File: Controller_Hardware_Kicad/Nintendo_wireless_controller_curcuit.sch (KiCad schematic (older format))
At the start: 23 parts, among them IC1 ATTINY2313-S, J1 BATT, J2 NRF_conn, U1 MAX1811, U2 LP5951MF-3.3, X1 USB-MB-S, X2 8MHz, sw1 CONN_2

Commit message: configured max1811 pin connections again.. and again
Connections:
- net +5V: now also U1.1 (SELV)
- net GND: no longer U1.1 (SELV)
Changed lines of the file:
@@
-EESchema Schematic File Version 2  date 19-06-2012 16:43:49
+EESchema Schematic File Version 2  date 19-06-2012 16:48:53
 LIBS:power
 LIBS:device
@@
 Comment4 ""
 $EndDescr
-Wire Wire Line
-	2550 7100 2550 6700
-Wire Wire Line
-	4450 7200 4800 7200
-Wire Wire Line
-	4800 7200 4800 7150
-Wire Wire Line
-	4800 6750 4800 6700
-Wire Wire Line
-	4800 6700 3900 6700
+$Comp
+L +5V #PWR01
+U 1 1 4FE08C10
+P 2550 6650
+F 0 "#PWR01" H 2550 6740 20  0001 C CNN
+F 1 "+5V" H 2550 6740 30  0000 C CNN
+	1    2550 6650
+	1    0    0    -1
+$EndComp
+Wire Wire Line
+	2550 6700 2550 6650
+Wire Wire Line
+	2550 7100 2550 6800
+Connection ~ 4450 7200
+Wire Wire Line
+	4450 7150 4450 7300
+Wire Wire Line
+	5150 4150 5150 4200
+Wire Wire Line
+	5150 4200 5200 4200
+Connection ~ 2600 3000
+Wire Wire Line
+	2800 3000 2350 3000
+Wire Wire Line
+	2800 3000 2800 3150
+Wire Wire Line
+	3300 850  3300 700
+Wire Wire Line
+	8300 2300 8300 2450
+Wire Wire Line
+	6750 2700 6750 2450
+Wire Wire Line
+	4450 3500 4450 3600
+Connection ~ 2600 3550
+Wire Wire Line
+	2800 3550 2350 3550
+Wire Wire Line
+	5150 4500 5150 4400
+Wire Wire Line
+	5150 4400 5200 4400
+Wire Wire Line
+	7150 6400 7550 6400
+Wire Wire Line
+	1500 5700 1500 5350
+Wire Wire Line
+	1500 5350 1300 5350
+Wire Wire Line
+	8300 2450 8050 2450
+Connection ~ 9750 5750
+Wire Wire Line
+	10150 5850 10150 5750
+Wire Wire Line
+	10150 5750 9750 5750
+Connection ~ 7950 6000
+Wire Wire Line
+	8100 6100 7950 6100
+Wire Wire Line
+	7550 5600 7550 5400
+Wire Wire Line
+	8900 6600 8900 6850
+Connection ~ 2150 5350
+Wire Wire Line
+	2150 5350 2700 5350
+Wire Wire Line
+	2150 6500 2700 6500
+Wire Wire Line
+	2150 6350 2150 6500
+Wire Wire Line
+	2150 5300 2150 5400
+Wire Wire Line
+	4450 6600 4450 6750
+Wire Wire Line
+	3900 7000 4000 7000
+Connection ~ 4000 7000
+Wire Wire Line
+	4000 7000 4000 7100
+Connection ~ 2550 6800
+Wire Wire Line
+	2550 6800 2700 6800
+Connection ~ 5700 7000
+Wire Wire Line
+	5700 7150 5700 6900
+Wire Wire Line
+	5350 7000 5700 7000
+Wire Wire Line
+	5700 6500 5700 6700
+Wire Wire Line
+	5700 6700 5800 6700
+Wire Wire Line
+	1750 5300 1750 5450
+Wire Wire Line
+	1750 5450 1300 5450
+Connection ~ 2400 1750
+Wire Wire Line
+	2300 1750 3200 1750
+Wire Wire Line
+	3200 1750 3200 2000
+Wire Wire Line
+	3200 2000 3300 2000
+Wire Wire Line
+	2400 1850 2400 1750
+Wire Wire Line
+	1900 2550 1750 2550
+Wire Wire Line
+	1750 1750 1900 1750
+Connection ~ 1750 2550
+Wire Wire Line
+	2400 2450 2400 2550
+Wire Wire Line
+	3300 2200 3200 2200
+Wire Wire Line
+	3200 2550 3200 2200
+Wire Wire Line
+	2300 2550 3200 2550
+Connection ~ 2400 2550
+Wire Wire Line
+	3300 1350 3300 1700
+Wire Wire Line
+	5700 6900 5800 6900
+Wire Wire Line
+	5350 6600 5700 6600
+Connection ~ 5700 6600
+Wire Wire Line
+	2700 6700 2550 6700
+Wire Wire Line
+	2550 7000 2700 7000
+Connection ~ 2550 7000
+Wire Wire Line
+	3900 6400 4000 6400
+Wire Wire Line
+	4000 6400 4000 6350
+Connection ~ 4450 6700
+Wire Wire Line
+	2150 5900 2150 5950
+Wire Wire Line
+	2700 5350 2700 6400
+Wire Wire Line
+	2050 6450 2150 6450
+Connection ~ 2150 6450
+Wire Wire Line
+	9750 6000 9700 6000
+Wire Wire Line
+	9750 5550 9750 6000
+Wire Wire Line
+	10150 6250 10150 6500
+Wire Wire Line
+	7550 6400 7550 6550
+Wire Wire Line
+	7550 6000 7550 5800
+Wire Wire Line
+	6750 2450 7250 2450
+Wire Wire Line
+	7950 6100 7950 6000
+Wire Wire Line
+	8100 6000 7150 6000
+Connection ~ 7550 6000
+Wire Wire Line
+	2600 3650 2600 3550
+Wire Wire Line
+	1750 2700 1750 1750
+Wire Wire Line
+	5600 5200 5650 5200
+Wire Wire Line
+	5650 5200 5650 5300
+Wire Wire Line
+	5600 5000 5650 5000
+Wire Wire Line
+	5650 5000 5650 4950
+Wire Wire Line
+	4450 1400 4450 1250
+Wire Wire Line
+	2350 3000 2350 3150
 Wire Wire Line
 	2600 3000 2600 2950
 Wire Wire Line
-	2350 3150 2350 3000
-Wire Wire Line
-	4450 1400 4450 1250
-Wire Wire Line
-	5650 4950 5650 5000
-Wire Wire Line
-	5650 5000 5600 5000
-Wire Wire Line
-	5650 5300 5650 5200
-Wire Wire Line
-	5650 5200 5600 5200
-Wire Wire Line
-	1750 2700 1750 1750
-Wire Wire Line
-	2600 3650 2600 3550
-Connection ~ 7550 6000
-Wire Wire Line
-	8100 6000 7150 6000
-Wire Wire Line
-	7950 6000 7950 6100
-Wire Wire Line
-	7250 2450 6750 2450
-Wire Wire Line
-	7550 6000 7550 5800
-Wire Wire Line
-	7550 6550 7550 6400
-Wire Wire Line
-	10150 6250 10150 6500
-Wire Wire Line
-	9750 5550 9750 6000
-Wire Wire Line
-	9750 6000 9700 6000
-Connection ~ 2150 6450
-Wire Wire Line
-	2050 6450 2150 6450
-Wire Wire Line
-	2700 6400 2700 5350
-Wire Wire Line
-	2150 5900 2150 5950
-Connection ~ 4450 6700
-Wire Wire Line
-	4000 6350 4000 6400
-Wire Wire Line
-	4000 6400 3900 6400
-Connection ~ 2550 7000
-Wire Wire Line
-	2550 7000 2700 7000
-Wire Wire Line
-	2550 6700 2700 6700
-Connection ~ 5700 6600
-Wire Wire Line
-	5350 6600 5700 6600
-Wire Wire Line
-	5800 6900 5700 6900
-Wire Wire Line
-	3300 1350 3300 1700
-Connection ~ 2400 2550
-Wire Wire Line
-	2300 2550 3200 2550
-Wire Wire Line
-	3200 2550 3200 2200
-Wire Wire Line
-	3200 2200 3300 2200
-Wire Wire Line
-	2400 2450 2400 2550
-Connection ~ 1750 2550
-Wire Wire Line
-	1750 1750 1900 1750
-Wire Wire Line
-	1900 2550 1750 2550
-Wire Wire Line
-	2400 1850 2400 1750
-Wire Wire Line
-	3300 2000 3200 2000
-Wire Wire Line
-	3200 2000 3200 1750
-Wire Wire Line
-	3200 1750 2300 1750
-Connection ~ 2400 1750
-Wire Wire Line
-	1300 5450 1750 5450
-Wire Wire Line
-	1750 5450 1750 5300
-Wire Wire Line
-	5800 6700 5700 6700
-Wire Wire Line
-	5700 6700 5700 6500
-Wire Wire Line
-	5350 7000 5700 7000
-Wire Wire Line
-	5700 6900 5700 7150
-Connection ~ 5700 7000
-Wire Wire Line
-	2550 6800 2700 6800
-Connection ~ 2550 6800
-Wire Wire Line
-	4000 7100 4000 7000
-Connection ~ 4000 7000
-Wire Wire Line
-	4000 7000 3900 7000
-Wire Wire Line
-	4450 6600 4450 6750
-Wire Wire Line
-	2150 5300 2150 5400
-Wire Wire Line
-	2150 6350 2150 6500
-Wire Wire Line
-	2150 6500 2700 6500
-Wire Wire Line
-	2700 5350 2150 5350
-Connection ~ 2150 5350
-Wire Wire Line
-	8900 6600 8900 6850
-Wire Wire Line
-	7550 5600 7550 5400
-Wire Wire Line
-	7950 6100 8100 6100
-Connection ~ 7950 6000
-Wire Wire Line
-	9750 5750 10150 5750
-Wire Wire Line
-	10150 5750 10150 5850
-Connection ~ 9750 5750
-Wire Wire Line
-	8050 2450 8300 2450
-Wire Wire Line
-	1300 5350 1500 5350
-Wire Wire Line
-	1500 5350 1500 5700
-Wire Wire Line
-	7550 6400 7150 6400
-Wire Wire Line
-	5200 4400 5150 4400
-Wire Wire Line
-	5150 4400 5150 4500
-Wire Wire Line
-	2800 3550 2350 3550
-Connection ~ 2600 3550
-Wire Wire Line
-	4450 3500 4450 3600
-Wire Wire Line
-	6750 2450 6750 2700
-Wire Wire Line
-	8300 2450 8300 2300
-Wire Wire Line
-	3300 850  3300 700
-Wire Wire Line
-	2800 3150 2800 3000
-Wire Wire Line
-	2800 3000 2350 3000
-Connection ~ 2600 3000
-Wire Wire Line
-	5200 4200 5150 4200
-Wire Wire Line
-	5150 4200 5150 4150
-Wire Wire Line
-	4450 7150 4450 7300
-Connection ~ 4450 7200
+	3900 6700 4800 6700
+Wire Wire Line
+	4800 6700 4800 6750
+Wire Wire Line
+	4800 7150 4800 7200
+Wire Wire Line
+	4800 7200 4450 7200
 Text Notes 2850 6150 0    60   ~ 0
 100mA charge current = ca. 4hr charge time

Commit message: ahmmaghad! we forgot to connect the dataline to the controller
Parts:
- added P1: CONN_1, symbol CONN_1
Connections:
- net at IC1.6 ((CKOUT/XCK/INT0)PD2): now also P1.1

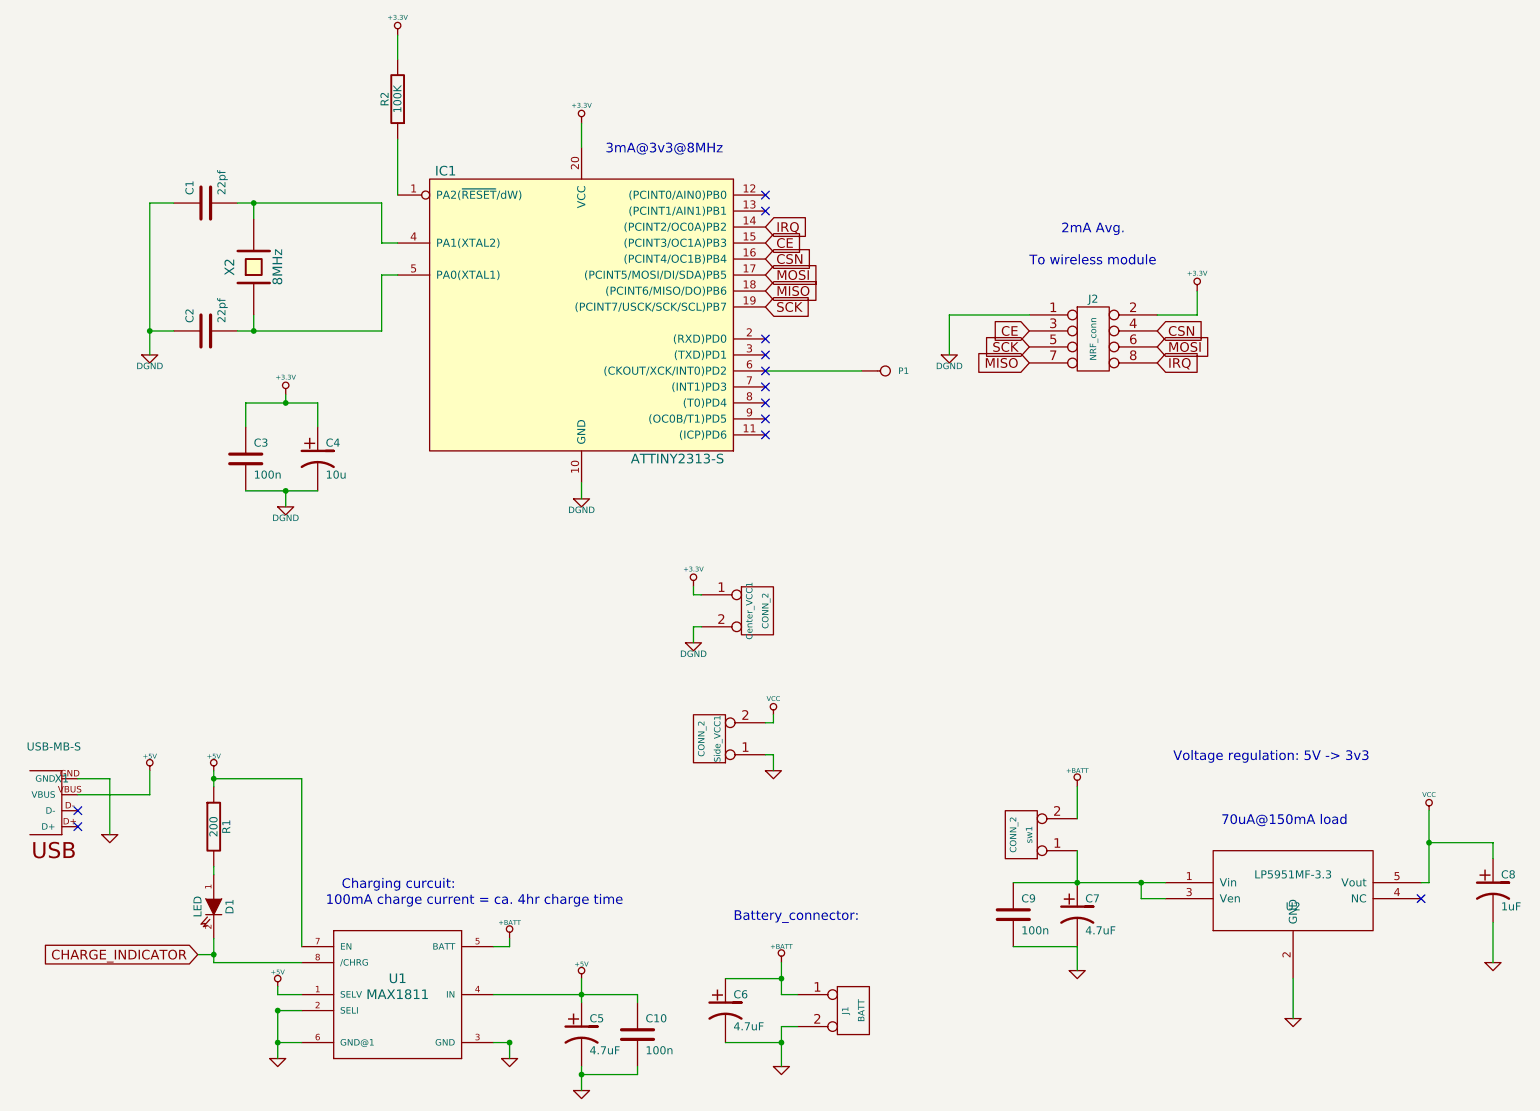
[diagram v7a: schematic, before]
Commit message: changed schematic to utilize attiny24 - still needs analog circuitry, netlisted and changed footprints, but didnt start layouting
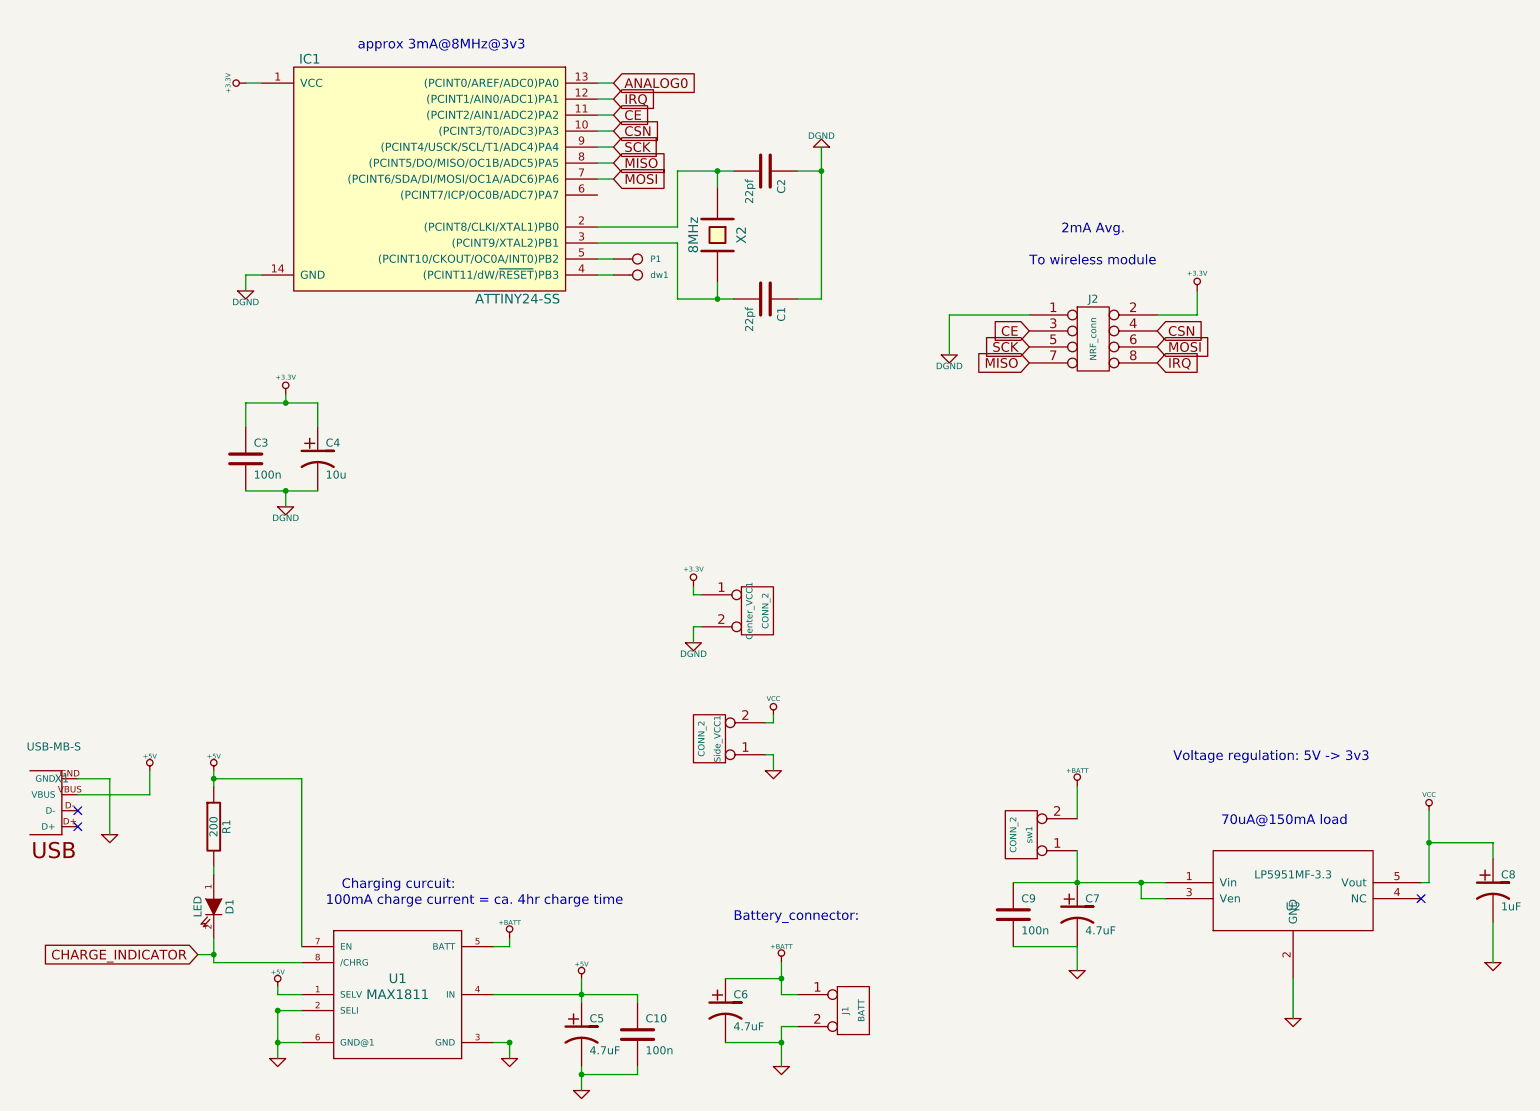
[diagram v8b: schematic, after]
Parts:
- removed IC1: ATTINY2313-S, SO20, symbol ATTINY2313-S
- removed R2: 100K, symbol R
- added IC1: ATTINY24-SS, SO14, symbol ATTINY24-SS
- added dw1: CONN_1, symbol CONN_1
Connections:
- net +3.3V: now also IC1.1 (VCC)
- net CE: now also IC1.11 ((PCINT2/AIN1/ADC2)PA2)
- net CSN: now also IC1.10 ((PCINT3/T0/ADC3)PA3)
- net DGND: now also IC1.14 (GND)
- net IRQ: now also IC1.12 ((PCINT1/AIN0/ADC1)PA1)
- net MISO: now also IC1.8 ((PCINT5/DO/MISO/OC1B/ADC5)PA5)
- net MOSI: now also IC1.7 ((PCINT6/SDA/DI/MOSI/OC1A/ADC6)PA6)
- net SCK: now also IC1.9 ((PCINT4/USCK/SCL/T1/ADC4)PA4)
- net at C1.2, X2.2: now also IC1.3 ((PCINT9/XTAL2)PB1)
- net at C2.2, X2.1: now also IC1.2 ((PCINT8/CLKI/XTAL1)PB0)
- net at P1.1: now also IC1.5 ((PCINT10/CKOUT/OC0A/INT0)PB2)
- new net: IC1.4 ((PCINT11/dW/~RESET~)PB3), dw1.1
- new net ANALOG0: IC1.13 ((PCINT0/AREF/ADC0)PA0)
- no-connect marks 12 -> 3
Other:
- note added: "approx 3mA@8MHz@3v3"
- note removed: "3mA@3v3@8MHz"
- moved on the sheet: C1, C2, X2
